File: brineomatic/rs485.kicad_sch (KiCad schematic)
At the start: 12 parts, among them J23 3.5mm, J24 3.5mm, U10 MAX3485

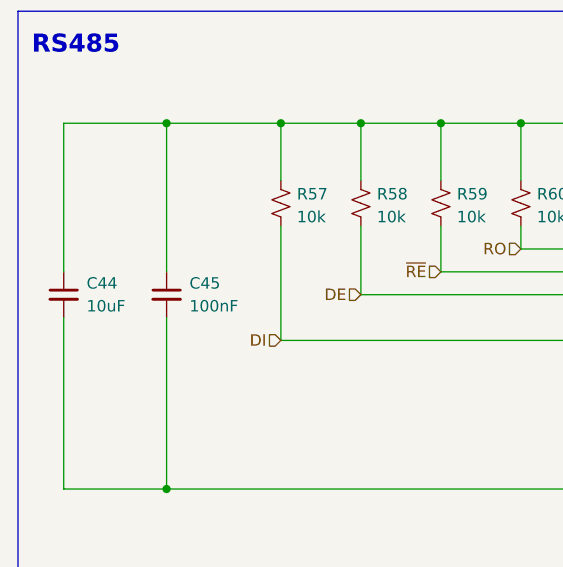
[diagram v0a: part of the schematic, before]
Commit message: tmc2209 add 470pF / 100v caps to outputs for esd protection
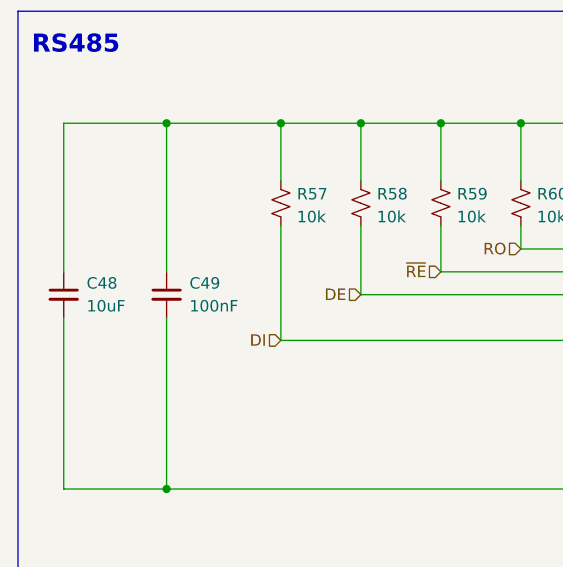
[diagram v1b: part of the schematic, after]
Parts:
- renumbered C44 to C48, C45 to C49
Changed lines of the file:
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@@
 		(on_board yes)
 		(dnp no)
-		(property "Reference" "C44"
+		(property "Reference" "C48"
 			(at 74.93 100.3363 0)
 			(effects
@@
 			(project "brineomatic"
 				(path "/96477ae2-ef08-48f3-8dd4-fe4478541f68/ecabf60a-7f79-4ba0-9fc6-a1e702c2d5f0"
-					(reference "C44")
+					(reference "C48")
 					(unit 1)
 				)
@@
 		(dnp no)
 		(fields_autoplaced yes)
-		(property "Reference" "C45"
+		(property "Reference" "C49"
 			(at 86.36 100.3363 0)
 			(effects
@@
 			(project "brineomatic"
 				(path "/96477ae2-ef08-48f3-8dd4-fe4478541f68/ecabf60a-7f79-4ba0-9fc6-a1e702c2d5f0"
-					(reference "C45")
-					(unit 1)
-				)
+					(reference "C49")
+					(unit 1)
+				)

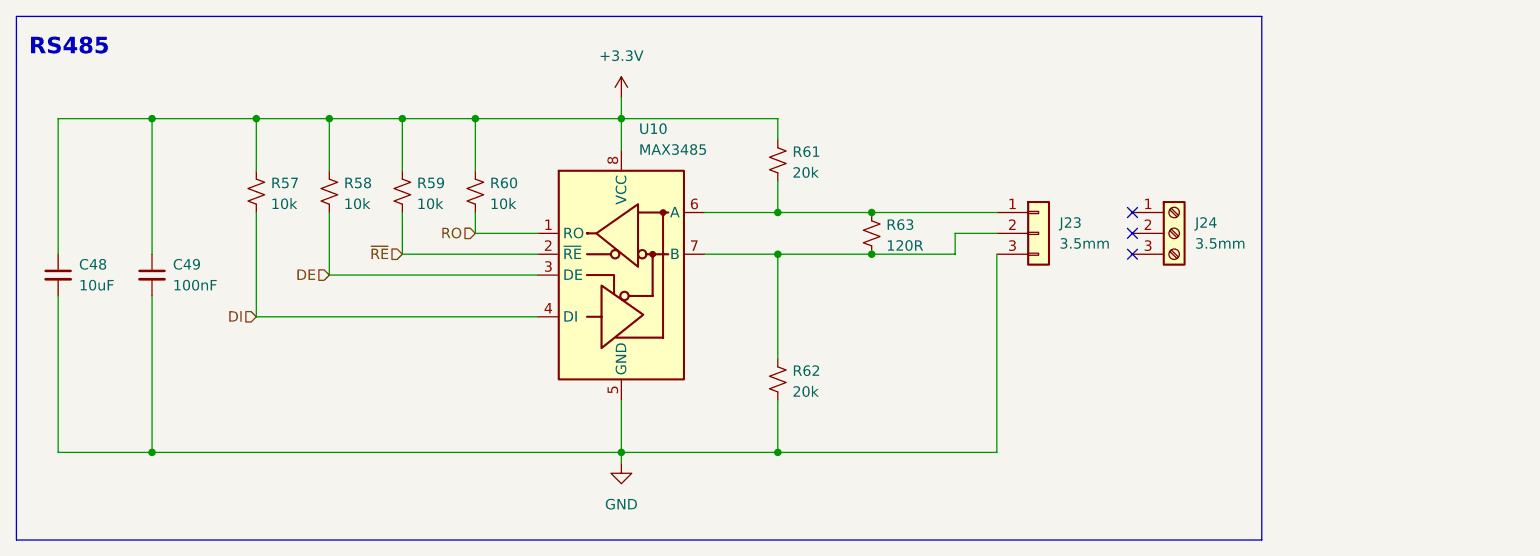
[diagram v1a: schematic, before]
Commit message: updated the modbus schematic with esd and DERE combination
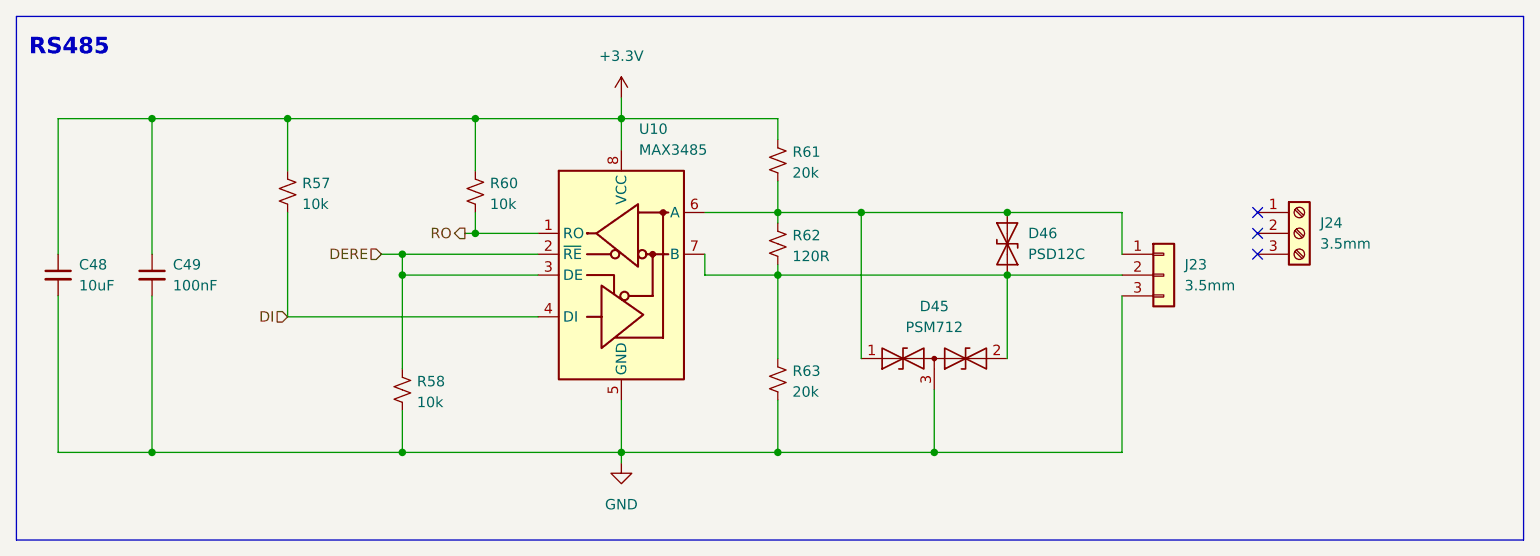
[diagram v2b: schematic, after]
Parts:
- removed R59: 10k, Resistor_SMD:R_0603_1608Metric, symbol Device:R_Small_US
- added D45: PSM712, Package_TO_SOT_SMD:SOT-23, symbol Diode:SM712_SOT23
- added D46: PSD12C, Diode_SMD:D_SOD-323, symbol Diode:SD12_SOD323
- renumbered R63 to R62, R62 to R63
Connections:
- net ~{RE} is gone; now on net DERE: U10.2 (~{RE})
- net +3.3V: no longer R58.2
- net GND: now also R58.1, D45.3 (common)
- net at J23.2 (Pin_2), R62.1, R63.2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: now also D45.2 (A2), D46.1 (A1)
- net at J23.1 (Pin_1), R61.1, R62.2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: now also D45.1 (A1), D46.2 (A2)
- net DE renamed DERE
- net DERE: now also R58.2; no longer R58.1
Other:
- moved on the sheet: J23, J24, R57, R58, R62

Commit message: add inline resistor to temperature sensor + servo inputs - 100ohm
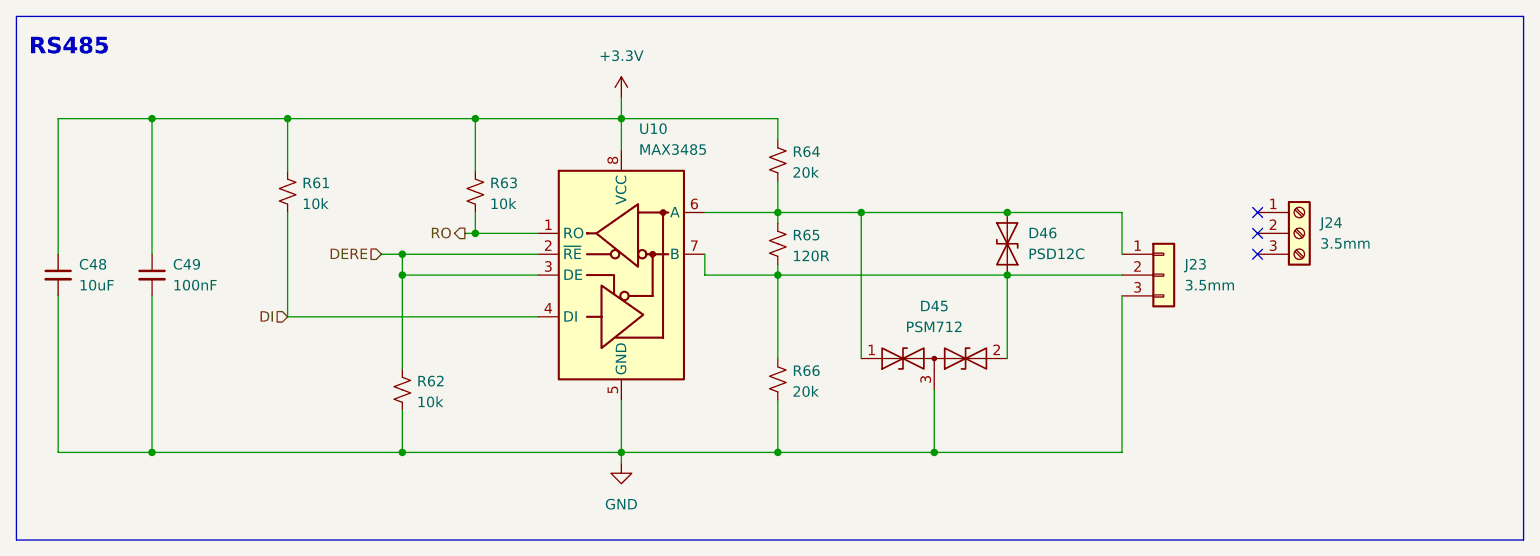
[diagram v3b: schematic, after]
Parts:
- renumbered R57 to R61, R58 to R62, R60 to R63, R61 to R64, R62 to R65, R63 to R66
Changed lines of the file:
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@@
 		(on_board yes)
 		(dnp no)
-		(property "Reference" "R63"
+		(property "Reference" "R66"
 			(at 161.798 113.284 0)
 			(effects
@@
 			(project "brineomatic"
 				(path "/96477ae2-ef08-48f3-8dd4-fe4478541f68/ecabf60a-7f79-4ba0-9fc6-a1e702c2d5f0"
-					(reference "R63")
+					(reference "R66")
 					(unit 1)
 				)
@@
 		(on_board yes)
 		(dnp no)
-		(property "Reference" "R57"
+		(property "Reference" "R61"
 			(at 102.108 90.424 0)
 			(effects
@@
 			(project "brineomatic"
 				(path "/96477ae2-ef08-48f3-8dd4-fe4478541f68/ecabf60a-7f79-4ba0-9fc6-a1e702c2d5f0"
-					(reference "R57")
+					(reference "R61")
 					(unit 1)
 				)
@@
 		(on_board yes)
 		(dnp no)
-		(property "Reference" "R60"
+		(property "Reference" "R63"
 			(at 124.968 90.424 0)
 			(effects
@@
 			(project "brineomatic"
 				(path "/96477ae2-ef08-48f3-8dd4-fe4478541f68/ecabf60a-7f79-4ba0-9fc6-a1e702c2d5f0"
-					(reference "R60")
+					(reference "R63")
 					(unit 1)
 				)
@@
 		(on_board yes)
 		(dnp no)
-		(property "Reference" "R62"
+		(property "Reference" "R65"
 			(at 161.798 96.774 0)
 			(effects
@@
 			(project "brineomatic"
 				(path "/96477ae2-ef08-48f3-8dd4-fe4478541f68/ecabf60a-7f79-4ba0-9fc6-a1e702c2d5f0"
-					(reference "R62")
+					(reference "R65")
 					(unit 1)
 				)
@@
 		(on_board yes)
 		(dnp no)
-		(property "Reference" "R58"
+		(property "Reference" "R62"
 			(at 116.078 114.554 0)
 			(effects
@@
 			(project "brineomatic"
 				(path "/96477ae2-ef08-48f3-8dd4-fe4478541f68/ecabf60a-7f79-4ba0-9fc6-a1e702c2d5f0"
-					(reference "R58")
+					(reference "R62")
 					(unit 1)
 				)
@@
 		(on_board yes)
 		(dnp no)
-		(property "Reference" "R61"
+		(property "Reference" "R64"
 			(at 161.798 86.614 0)
 			(effects
@@
 			(project "brineomatic"
 				(path "/96477ae2-ef08-48f3-8dd4-fe4478541f68/ecabf60a-7f79-4ba0-9fc6-a1e702c2d5f0"
-					(reference "R61")
-					(unit 1)
-				)
+					(reference "R64")
+					(unit 1)
+				)

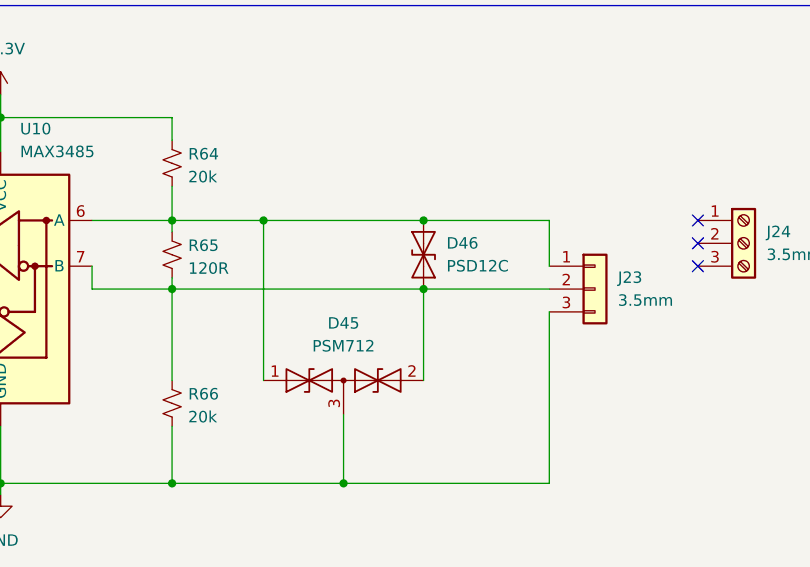
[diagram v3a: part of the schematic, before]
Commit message: updated analog sensor esd schematic
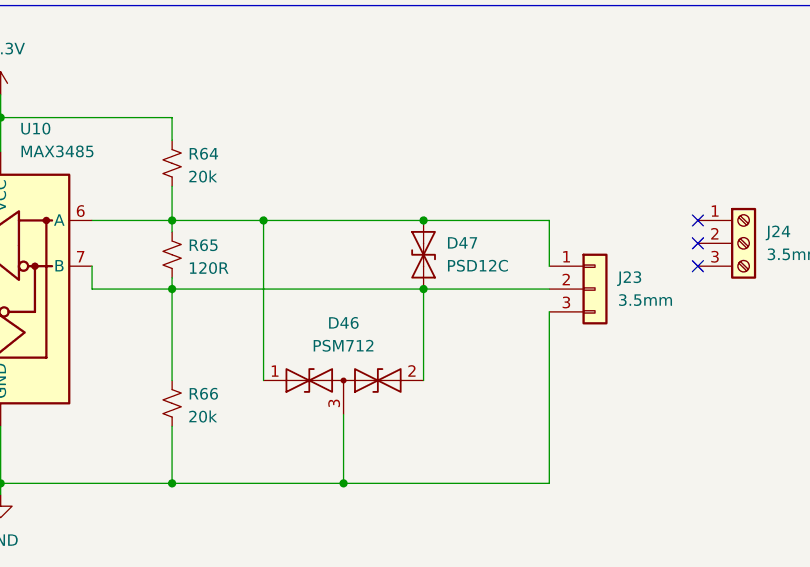
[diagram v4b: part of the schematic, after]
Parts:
- renumbered D45 to D46, D46 to D47
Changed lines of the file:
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@@
 		(dnp no)
 		(fields_autoplaced yes)
-		(property "Reference" "#PWR069"
+		(property "Reference" "#PWR070"
 			(at 140.97 130.81 0)
 			(effects
@@
 			(project "brineomatic"
 				(path "/96477ae2-ef08-48f3-8dd4-fe4478541f68/ecabf60a-7f79-4ba0-9fc6-a1e702c2d5f0"
-					(reference "#PWR069")
+					(reference "#PWR070")
 					(unit 1)
 				)
@@
 		(dnp no)
 		(fields_autoplaced yes)
-		(property "Reference" "D46"
+		(property "Reference" "D47"
 			(at 190.5 96.5199 90)
 			(effects
@@
 			(project ""
 				(path "/96477ae2-ef08-48f3-8dd4-fe4478541f68/ecabf60a-7f79-4ba0-9fc6-a1e702c2d5f0"
-					(reference "D46")
+					(reference "D47")
 					(unit 1)
 				)
@@
 		(dnp no)
 		(fields_autoplaced yes)
-		(property "Reference" "D45"
+		(property "Reference" "D46"
 			(at 179.07 105.41 0)
 			(effects
@@
 			(project ""
 				(path "/96477ae2-ef08-48f3-8dd4-fe4478541f68/ecabf60a-7f79-4ba0-9fc6-a1e702c2d5f0"
-					(reference "D45")
+					(reference "D46")
 					(unit 1)
 				)
@@
 		(dnp no)
 		(fields_autoplaced yes)
-		(property "Reference" "#PWR068"
+		(property "Reference" "#PWR069"
 			(at 140.97 83.82 0)
 			(effects
@@
 			(project ""
 				(path "/96477ae2-ef08-48f3-8dd4-fe4478541f68/ecabf60a-7f79-4ba0-9fc6-a1e702c2d5f0"
-					(reference "#PWR068")
-					(unit 1)
-				)
+					(reference "#PWR069")
+					(unit 1)
+				)

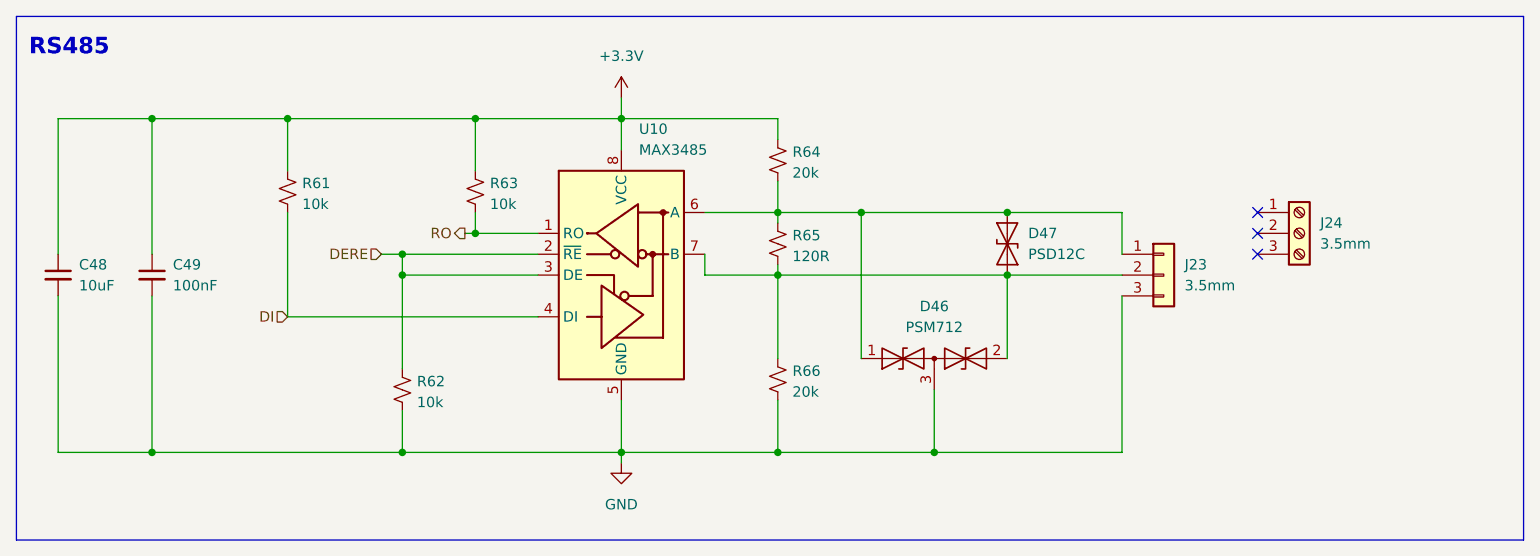
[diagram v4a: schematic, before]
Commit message: added bulk cap after ideal diode
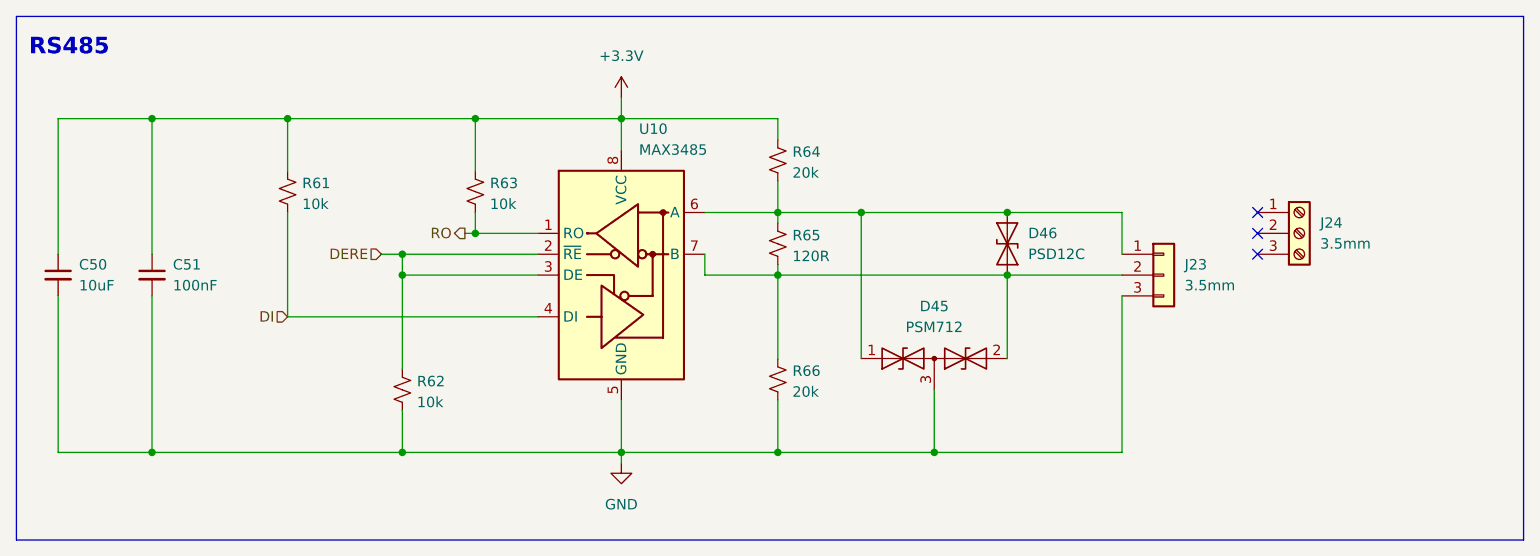
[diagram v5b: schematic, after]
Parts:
- renumbered C48 to C50, C49 to C51, D46 to D45, D47 to D46
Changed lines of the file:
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@@
 		(dnp no)
 		(fields_autoplaced yes)
-		(property "Reference" "#PWR070"
+		(property "Reference" "#PWR072"
 			(at 140.97 130.81 0)
 			(effects
@@
 			(project "brineomatic"
 				(path "/96477ae2-ef08-48f3-8dd4-fe4478541f68/ecabf60a-7f79-4ba0-9fc6-a1e702c2d5f0"
-					(reference "#PWR070")
+					(reference "#PWR072")
 					(unit 1)
 				)
@@
 		(dnp no)
 		(fields_autoplaced yes)
-		(property "Reference" "D47"
+		(property "Reference" "D46"
 			(at 190.5 96.5199 90)
 			(effects
@@
 			(project ""
 				(path "/96477ae2-ef08-48f3-8dd4-fe4478541f68/ecabf60a-7f79-4ba0-9fc6-a1e702c2d5f0"
-					(reference "D47")
+					(reference "D46")
 					(unit 1)
 				)
@@
 		(dnp no)
 		(fields_autoplaced yes)
-		(property "Reference" "D46"
+		(property "Reference" "D45"
 			(at 179.07 105.41 0)
 			(effects
@@
 			(project ""
 				(path "/96477ae2-ef08-48f3-8dd4-fe4478541f68/ecabf60a-7f79-4ba0-9fc6-a1e702c2d5f0"
-					(reference "D46")
+					(reference "D45")
 					(unit 1)
 				)
@@
 		(on_board yes)
 		(dnp no)
-		(property "Reference" "C48"
+		(property "Reference" "C50"
 			(at 74.93 100.3363 0)
 			(effects
@@
 			(project "brineomatic"
 				(path "/96477ae2-ef08-48f3-8dd4-fe4478541f68/ecabf60a-7f79-4ba0-9fc6-a1e702c2d5f0"
-					(reference "C48")
+					(reference "C50")
 					(unit 1)
 				)
@@
 		(dnp no)
 		(fields_autoplaced yes)
-		(property "Reference" "C49"
+		(property "Reference" "C51"
 			(at 86.36 100.3363 0)
 			(effects
@@
 			(project "brineomatic"
 				(path "/96477ae2-ef08-48f3-8dd4-fe4478541f68/ecabf60a-7f79-4ba0-9fc6-a1e702c2d5f0"
-					(reference "C49")
+					(reference "C51")
 					(unit 1)
 				)
@@
 		(dnp no)
 		(fields_autoplaced yes)
-		(property "Reference" "#PWR069"
+		(property "Reference" "#PWR071"
 			(at 140.97 83.82 0)
 			(effects
@@
 			(project ""
 				(path "/96477ae2-ef08-48f3-8dd4-fe4478541f68/ecabf60a-7f79-4ba0-9fc6-a1e702c2d5f0"
-					(reference "#PWR069")
-					(unit 1)
-				)
+					(reference "#PWR071")
+					(unit 1)
+				)

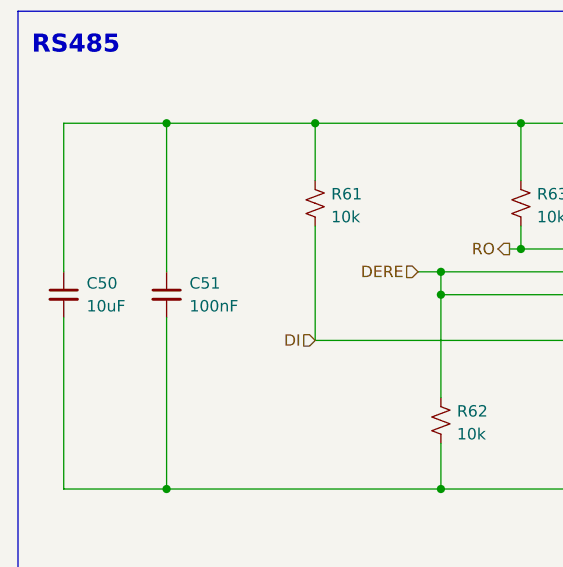
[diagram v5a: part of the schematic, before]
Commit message: added more input/output caps
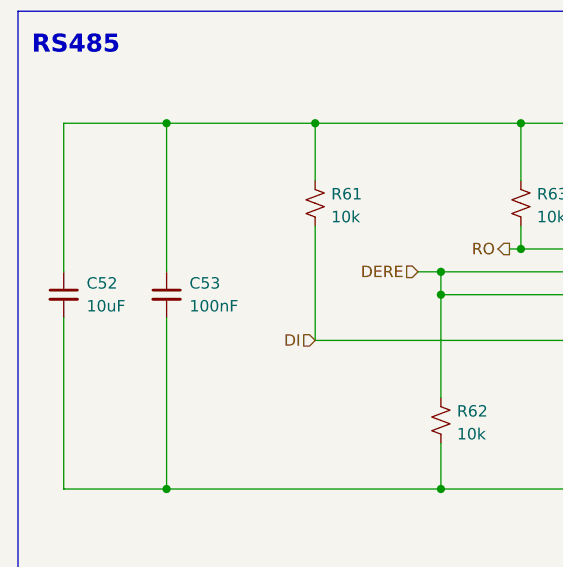
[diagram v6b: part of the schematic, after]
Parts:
- renumbered C50 to C52, C51 to C53
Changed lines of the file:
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@@
 		(on_board yes)
 		(dnp no)
-		(property "Reference" "C50"
+		(property "Reference" "C52"
 			(at 74.93 100.3363 0)
 			(effects
@@
 			(project "brineomatic"
 				(path "/96477ae2-ef08-48f3-8dd4-fe4478541f68/ecabf60a-7f79-4ba0-9fc6-a1e702c2d5f0"
-					(reference "C50")
+					(reference "C52")
 					(unit 1)
 				)
@@
 		(dnp no)
 		(fields_autoplaced yes)
-		(property "Reference" "C51"
+		(property "Reference" "C53"
 			(at 86.36 100.3363 0)
 			(effects
@@
 			(project "brineomatic"
 				(path "/96477ae2-ef08-48f3-8dd4-fe4478541f68/ecabf60a-7f79-4ba0-9fc6-a1e702c2d5f0"
-					(reference "C51")
+					(reference "C53")
 					(unit 1)
 				)

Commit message: added 1uF cap to pressure sensor connectors for esd
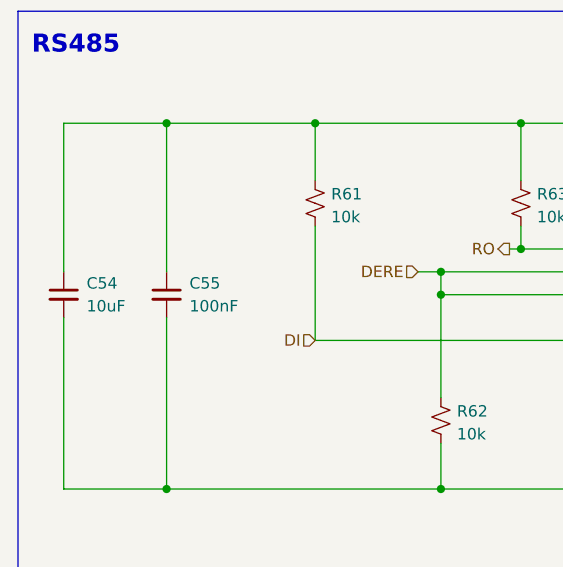
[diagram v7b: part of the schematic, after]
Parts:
- renumbered C52 to C54, C53 to C55
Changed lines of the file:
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@@
 		(on_board yes)
 		(dnp no)
-		(property "Reference" "C52"
+		(property "Reference" "C54"
 			(at 74.93 100.3363 0)
 			(effects
@@
 			(project "brineomatic"
 				(path "/96477ae2-ef08-48f3-8dd4-fe4478541f68/ecabf60a-7f79-4ba0-9fc6-a1e702c2d5f0"
-					(reference "C52")
+					(reference "C54")
 					(unit 1)
 				)
@@
 		(dnp no)
 		(fields_autoplaced yes)
-		(property "Reference" "C53"
+		(property "Reference" "C55"
 			(at 86.36 100.3363 0)
 			(effects
@@
 			(project "brineomatic"
 				(path "/96477ae2-ef08-48f3-8dd4-fe4478541f68/ecabf60a-7f79-4ba0-9fc6-a1e702c2d5f0"
-					(reference "C53")
+					(reference "C55")
 					(unit 1)
 				)
